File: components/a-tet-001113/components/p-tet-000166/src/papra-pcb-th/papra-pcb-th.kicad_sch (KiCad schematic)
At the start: 37 parts, among them Q1 P-FET, Q2 N-FET, Q3 N-FET, U1 QT Py ESP32-S3

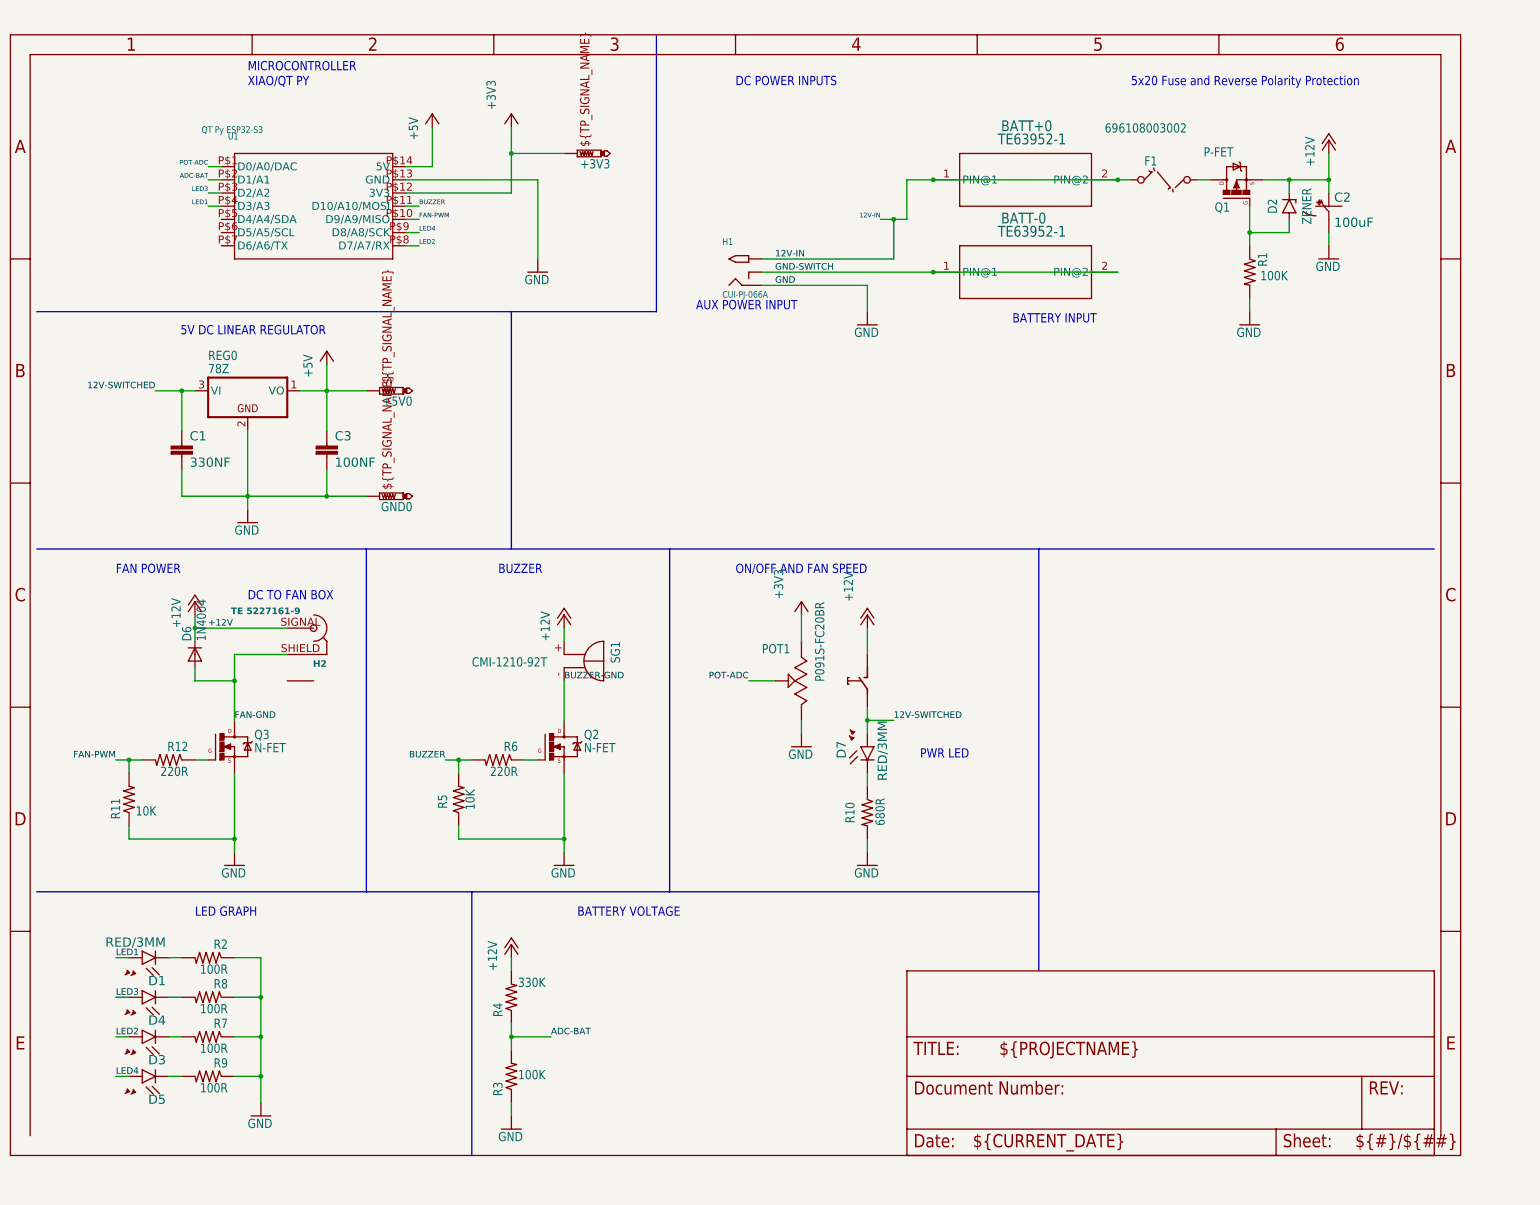
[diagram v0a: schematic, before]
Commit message: finally getting this work done after work done at OC MakerFaire. Also now has tests! idk if those are helpful since the orientation of many components still required hand-based edits
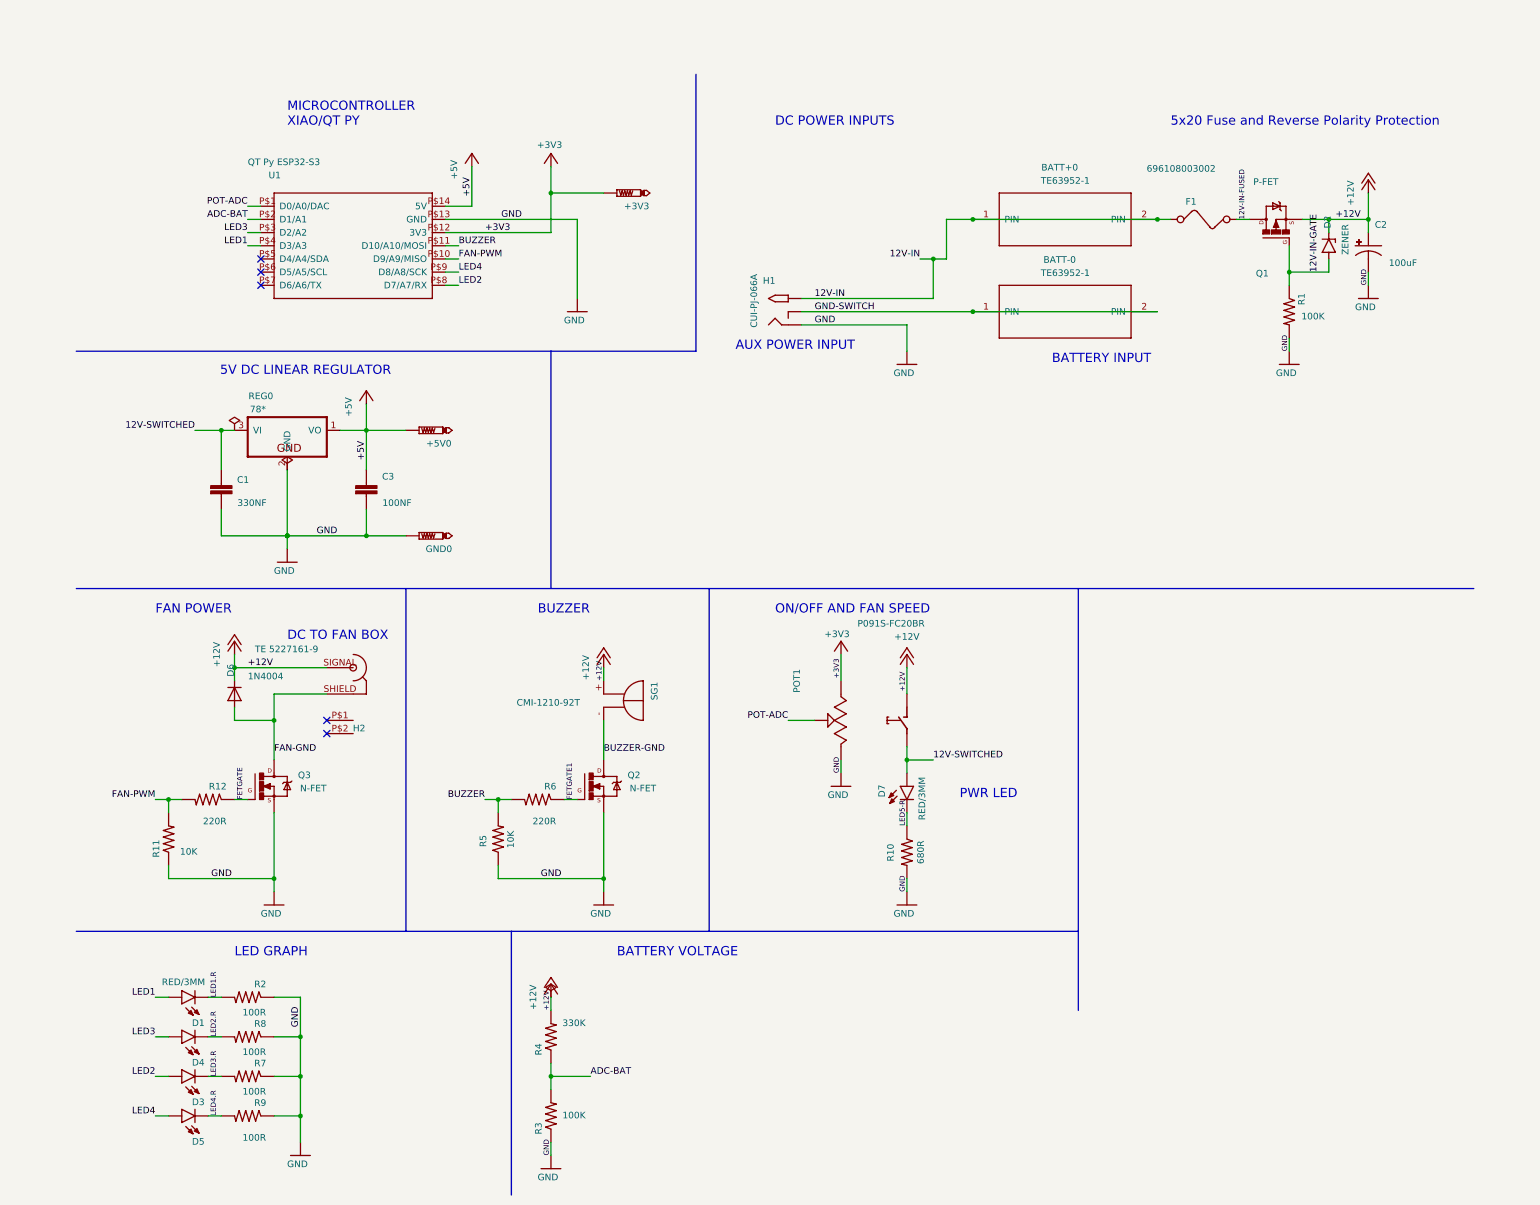
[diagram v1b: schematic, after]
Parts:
- removed +3V3, +5V0, GND0: PTR1PAD1-17, Papra TH_eagle:P1-17, symbol Papra TH_eagle-eagle-import:testpad_385_PTR1PAD1-17
- removed BATT+0, BATT-0: TE63952-1, Papra TH_eagle:TE63952-1, symbol Papra TH_eagle-eagle-import:PC-LIB_TE63952-1
- removed C1: 330NF, Papra TH_eagle:CAP-PTH-SMALL-KIT, symbol Papra TH_eagle-eagle-import:SparkFun-Capacitors_510_0.1UF-KIT-EZ-50V-20%
- removed C2: 100uF, Papra TH_eagle:CPOL-RADIAL-2.5MM-6.5MM, symbol Papra TH_eagle-eagle-import:SparkFun-Capacitors_510_100UF-POLAR-RADIAL-2.5MM-25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
- removed C3: 100NF, Papra TH_eagle:CAP-PTH-SMALL-KIT, symbol Papra TH_eagle-eagle-import:SparkFun-Capacitors_510_0.1UF-KIT-EZ-50V-20%
- removed D1, D3, D4, D5, D7: RED/3MM, Papra TH_eagle:LED_3MM, symbol Papra TH_eagle-eagle-import:SparkFun-LED_529_LED3MM
- removed D2: ZENER, Papra TH_eagle:DIODE-AXIAL, symbol Papra TH_eagle-eagle-import:Tinkercad_30890021_ZENER_DIODE-AXIAL
- removed D6: 1N4004, Papra TH_eagle:DO41-10, symbol Papra TH_eagle-eagle-import:adafruit_420_1N4004
- removed F1: 696108003002, Papra TH_eagle:FUSE, symbol Papra TH_eagle-eagle-import:special_367_FUSE
- removed H1: CUI-PJ-066A, Papra TH_eagle:DCJACK-PJ-066A-SLOT, symbol Papra TH_eagle-eagle-import:PC-LIB_CUI-PJ-066ASLOTTED
- removed H2: TE 5227161-9, Papra TH_eagle:TE-BNC, symbol Papra TH_eagle-eagle-import:PC-LIB_TE-BNC
- removed POT1: P091S-FC20BR, Papra TH_eagle:P091S-FC20BR, symbol Papra TH_eagle-eagle-import:PC-LIB_P091S-FC20BR
- removed Q1: P-FET, Papra TH_eagle:TO220BV, symbol Papra TH_eagle-eagle-import:Tinkercad_30890021_PMOSFET_TO220
- removed Q2, Q3: N-FET, Papra TH_eagle:TO220BV, symbol Papra TH_eagle-eagle-import:Transistor_16378713_NMOSFETTO220
- removed R1, R3: 100K, Papra TH_eagle:0207_10, symbol Papra TH_eagle-eagle-import:rcl_334_R-US_0207/10
- removed R10: 680R, Papra TH_eagle:0207_10, symbol Papra TH_eagle-eagle-import:rcl_334_R-US_0207/10
- removed R11, R5: 10K, Papra TH_eagle:0207_10, symbol Papra TH_eagle-eagle-import:rcl_334_R-US_0207/10
- removed R12, R6: 220R, Papra TH_eagle:0207_10, symbol Papra TH_eagle-eagle-import:rcl_334_R-US_0207/10
- removed R2, R7, R8, R9: 100R, Papra TH_eagle:0207_10, symbol Papra TH_eagle-eagle-import:rcl_334_R-US_0207/10
- removed R4: 330K, Papra TH_eagle:0207_10, symbol Papra TH_eagle-eagle-import:rcl_334_R-US_0207/10
- removed REG0: 78Z, Papra TH_eagle:TO92, symbol Papra TH_eagle-eagle-import:adafruit_420_78Z
- removed SG1: CMI-1210-92T, Papra TH_eagle:F_TMB, symbol Papra TH_eagle-eagle-import:buzzer_113_F/TMB
- removed U1: QT Py ESP32-S3, Papra TH_eagle:MODULE14P-TH+PAD, symbol Papra TH_eagle-eagle-import:Seeeduino-XIAO-footprint-eagle_MOUDLE-SEEEDUINO-XIA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
- added +3V3, +5V0, GND0: PTR1, papra-pcb-th:P1-17, symbol papra-pcb-th:PTR1_PAD1-17
- added BATT+0, BATT-0: TE63952-1, papra-pcb-th:TE63952-1, symbol papra-pcb-th:TE63952-1
- added C1: 330NF, papra-pcb-th:CAP-PTH-SMALL-KIT, symbol papra-pcb-th:0.1UF_-KIT-EZ-50V-20_
- added C2: 100uF, papra-pcb-th:CPOL-RADIAL-2.5MM-6.5MM, symbol papra-pcb-th:100UF-POLAR_-RADIAL-2.5MM-25V-20_
- added C3: 100NF, papra-pcb-th:CAP-PTH-SMALL-KIT, symbol papra-pcb-th:0.1UF_-KIT-EZ-50V-20_
- added D1, D3, D4, D5, D7: RED/3MM, papra-pcb-th:LED_3MM, symbol papra-pcb-th:LED_3MM
- added D2: ZENER, papra-pcb-th:DIODE-AXIAL, symbol papra-pcb-th:ZENER__DIODE-AXIAL
- added D6: 1N4004, papra-pcb-th:DO41-10, symbol papra-pcb-th:1N4004
- added F1: 696108003002, papra-pcb-th:FUSE, symbol papra-pcb-th:FUSE
- added H1: CUI-PJ-066A, papra-pcb-th:DCJACK-PJ-066A-SLOT, symbol papra-pcb-th:CUI-PJ-066A_SLOTTED
- added H2: TE 5227161-9, papra-pcb-th:TE-BNC, symbol papra-pcb-th:TE-BNC
- added POT1: P091S-FC20BR, papra-pcb-th:P091S-FC20BR, symbol papra-pcb-th:P091S-FC20BR
- added Q1: P-FET, papra-pcb-th:TO220BV, symbol papra-pcb-th:PMOSFET__TO220
- added Q2, Q3: N-FET, papra-pcb-th:TO220BV, symbol papra-pcb-th:NMOSFET_TO220
- added R1, R3: 100K, papra-pcb-th:0207_10, symbol papra-pcb-th:R-US__0207_10
- added R10: 680R, papra-pcb-th:0207_10, symbol papra-pcb-th:R-US__0207_10
- added R11, R5: 10K, papra-pcb-th:0207_10, symbol papra-pcb-th:R-US__0207_10
- added R12, R6: 220R, papra-pcb-th:0207_10, symbol papra-pcb-th:R-US__0207_10
- added R2, R7, R8, R9: 100R, papra-pcb-th:0207_10, symbol papra-pcb-th:R-US__0207_10
- added R4: 330K, papra-pcb-th:0207_10, symbol papra-pcb-th:R-US__0207_10
- added REG0: 78*, papra-pcb-th:TO92, symbol papra-pcb-th:78__Z
- added SG1: CMI-1210-92T, papra-pcb-th:F_TMB, symbol papra-pcb-th:F_TMB
- added U1: QT Py ESP32-S3, papra-pcb-th:MODULE14P-TH+PAD, symbol papra-pcb-th:MOUDLE-SEEEDUINO-XIAO_THRUHOLE+CASTELLATION
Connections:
- net +12V: now also C2.1 (+), D2.2 (C), D6.C, H2.SIGNAL (P1), POT1.COM (4), Q1.S, R4.2, SG1.+
- net +3V3: now also +3V3.TP, POT1.3, U1.P$12 (3V3)
- net +5V: now also +5V0.TP, C3.1, REG0.1 (VO), U1.P$14 (5V)
- net 12V-IN: now also BATT+0.1 (PIN), BATT+0.2 (PIN), F1.1, H1.PWR (TIP)
- net 12V-SWITCHED: now also C1.1, D7.A, POT1.NO (5), REG0.3 (VI)
- net ADC-BAT: now also R3.2, R4.1, U1.P$2 (D1/A1)
- net BUZZER: now also R5.2, R6.2, U1.P$11 (D10/A10/MOSI)
- net BUZZER-GND: now also Q2.D, SG1.-
- net FAN-GND: now also D6.A, H2.SHIELD (P2), Q3.D
- net FAN-PWM: now also R11.2, R12.2, U1.P$10 (D9/A9/MISO)
- net GND: now also C1.2, C2.2 (-), C3.2, GND0.TP, H1.GND (RING), POT1.1, Q2.S, Q3.S, R1.2, R10.2, R11.1, R2.1, R3.1, R5.1, R7.1, R8.1, R9.1, REG0.2 (GND), U1.P$13 (GND)
- net GND-SWITCH: now also BATT-0.1 (PIN), BATT-0.2 (PIN), H1.GNDBREAK (RING_SW)
- net LED1: now also D1.A, U1.P$4 (D3/A3)
- net LED2: now also D3.A, U1.P$8 (D7/A7/RX)
- net LED3: now also D4.A, U1.P$3 (D2/A2)
- net LED4: now also D5.A, U1.P$9 (D8/A8/SCK)
- net POT-ADC: now also POT1.2, U1.P$1 (D0/A0/DAC)
- new net 12V-IN-FUSED: F1.2, Q1.D
- new net 12V-IN-GATE: D2.1 (A), Q1.G, R1.1
- new net FETGATE: Q3.G, R12.1
- new net FETGATE1: Q2.G, R6.1
- new net LED1.R: D1.K (C), R2.2
- new net LED2.R: D4.K (C), R8.2
- new net LED3.R: D3.K (C), R7.2
- new net LED4.R: D5.K (C), R9.2
- new net LED5-R: D7.K (C), R10.1
- no-connect marks 0 -> 5
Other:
- company: (none) -> Tetra Bio Distributed
- title: (none) -> PAPRa M12 Controller PCB, Through-Hole (P-TET-000166)
